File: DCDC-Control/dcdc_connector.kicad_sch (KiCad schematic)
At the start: 0 parts

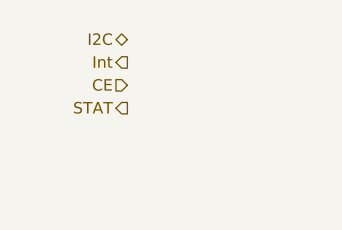
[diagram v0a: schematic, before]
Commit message: almost finished control schematics
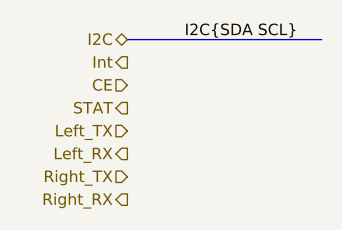
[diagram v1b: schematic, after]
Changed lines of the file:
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@@
 	(generator_version "9.0")
 	(paper "A4")
+	(bus
+		(pts
+			(xy 116.84 71.12) (xy 138.43 71.12)
+		)
+		(stroke
+			(width 0)
+			(type default)
+		)
+	)
+	(label "I2C{SDA SCL}"
+		(at 123.19 71.12 0)
+		(effects
+			(font
+				(size 1.27 1.27)
+			)
+			(justify left bottom)
+		)
+	)
+	(hierarchical_label "Right_RX"
+		(shape output)
+		(at 116.84 88.9 180)
+		(effects
+			(font
+				(size 1.27 1.27)
+			)
+			(justify right)
+		)
+	)
 	(hierarchical_label "STAT"
 		(shape output)
 		(at 116.84 78.74 180)
+		(effects
+			(font
+				(size 1.27 1.27)
+			)
+			(justify right)
+		)
+	)
+	(hierarchical_label "Left_RX"
+		(shape output)
+		(at 116.84 83.82 180)
 		(effects
 			(font
@@
 		(effects
 			(font
+				(size 1.27 1.27)
+			)
+			(justify right)
+		)
+	)
+	(hierarchical_label "Left_TX"
+		(shape input)
+		(at 116.84 81.28 180)
+		(effects
+			(font
+				(size 1.27 1.27)
+			)
+			(justify right)
+		)
+	)
+	(hierarchical_label "Right_TX"
+		(shape input)
+		(at 116.84 86.36 180)
+		(effects
+			(font
